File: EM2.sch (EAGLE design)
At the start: 114 parts, among them IC1 EUP3476SO08T, IC2 APX811-44UG-7, IC3 ATMEGA16U2-MU, IC4 MCP24AA025E48, IC6 W5500, IC9 ATMEGA2560-16AU, J1 DC_2_1MM, P1 USB-6PSMT, P3 ICSP:USB, P4 microSD, Q2 2N7002, U1 HY931147C-RJ45, X1 16MHz, X2 25MHz, X3 16MHz

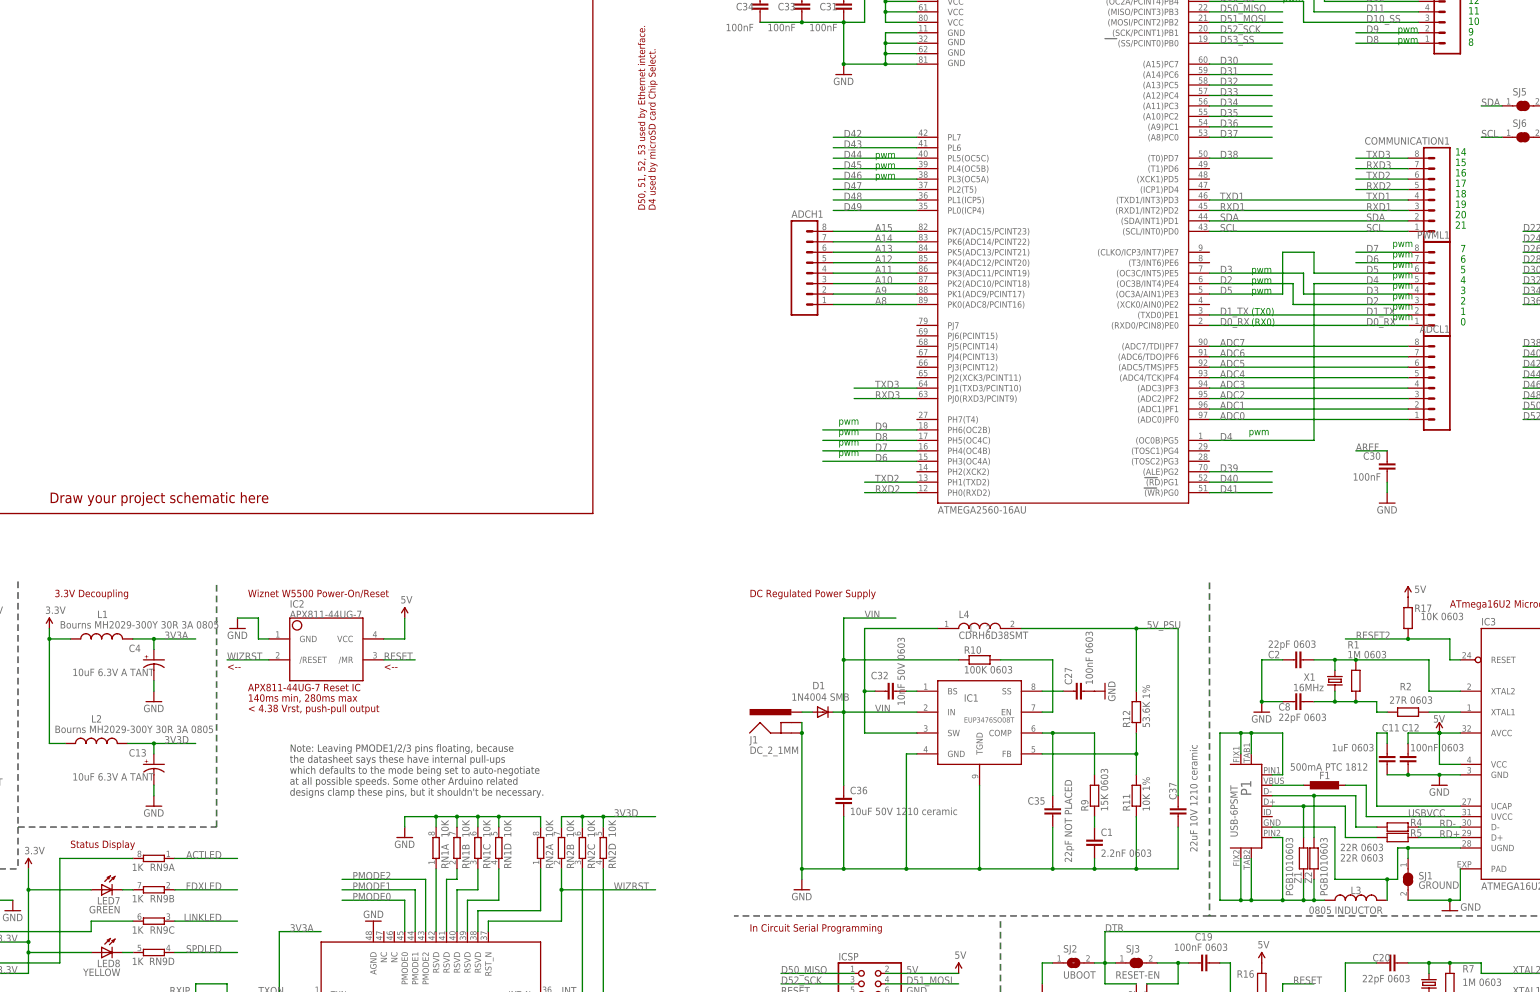
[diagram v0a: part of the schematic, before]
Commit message: Changed USB socket
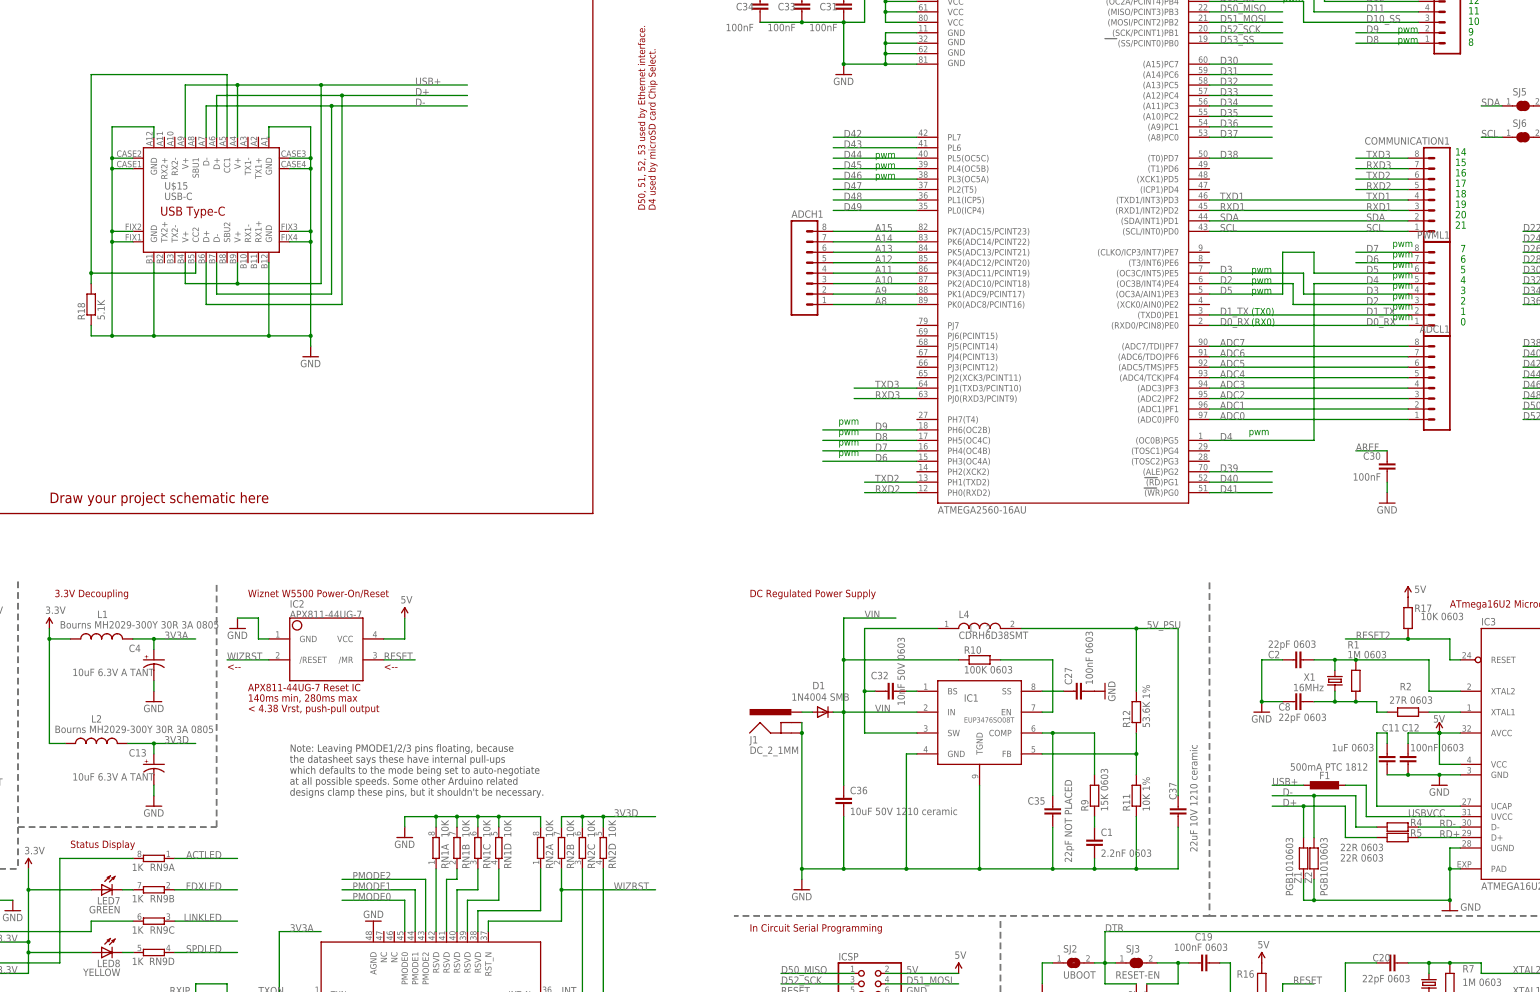
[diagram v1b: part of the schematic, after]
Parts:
- removed L3: 0805 INDUCTOR, freetronics-master-v1:INDUCTOR0805-LARGE
- removed P1: USB-6PSMT, freetronics-jon:USB-6PSMT
- removed SJ1: GROUND, freetronics-jon:SJCN
- added R18: 5.1K, freetronics-original:RESISTOR0603
- added U$15: USB-C, freetronics-jon:USB-C
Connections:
- removed net N$115: F1.1, P1.VBUS
- removed net N$16: P1.D+, R5.2, Z1.1
- removed net N$17: P1.D-, R4.2, Z2.1
- removed net N$18: L3.1, P1.FIX1, P1.FIX2, P1.PIN1, P1.PIN2, P1.TAB1, P1.TAB2, Z1.2, Z2.2
- removed net N$74: IC3.UGND, L3.2, P1.GND, SJ1.1
- new net D+: R5.2, U$15.D+@A6, U$15.D+@B6, Z1.1
- new net D-: R4.2, U$15.D-@A7, U$15.D-@B7, Z2.1
- new net N$67: R18.2, U$15.CC1, U$15.CC2
- new net USB+: F1.1, U$15.V+@A4, U$15.V+@A9, U$15.V+@B4, U$15.V+@B9
- net GND: now also IC3.UGND, R18.1, U$15.GND@A1, U$15.GND@A12, U$15.GND@B1, U$15.GND@B12, U$15.GND@CASE1, U$15.GND@CASE2, U$15.GND@CASE3, U$15.GND@CASE4, U$15.GND@FIX1, U$15.GND@FIX2, U$15.GND@FIX3, U$15.GND@FIX4, Z1.2, Z2.2; no longer SJ1.2

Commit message: Library part migration to SuperHouse
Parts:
- added R19: 5.1K, SuperHouse-DiscreteSemi:RESISTOR0603
- ADCH1, ADCL1, COMMUNICATION1, JP6, PWML1: value (none) -> M08-SOCKET; device freetronics-master-v1.1:M08STD -> SuperHouse-Connectors:M08-SOCKET
- C1, C12, C15, C16, C19, C2, C20, C21, C22, C23, C24, C27, C29, C30, C31, C32, C33, C34, C35, C7, C8, C9: device freetronics-marc:CAP0603 -> SuperHouse-DiscreteSemi:CAP0603
- C11: device freetronics-master-v1:CAP0603 -> SuperHouse-DiscreteSemi:CAP0603
- C14, C17, C5: device freetronics-jon:CAP0603 -> SuperHouse-DiscreteSemi:CAP0603
- D1: value 1N4004 SMB -> 1N4004 SMA; device freetronics:DIODESMB -> SuperHouse-DiscreteSemi:DIODESMA
- F1: device rcl:L-EUL1812 -> SuperHouse-Fuses:PTC050
- IC6: device W5500:W5500 -> SuperHouse-ICs:W5500
- IC9: device atmel-2005:ATMEGA1280-16AU -> SuperHouse-MCUs:ATMEGA25602560-16AU
- ICSP, P3: device pinhead:PINHD-2X3 -> SuperHouse-Connectors:ICSP-PIN
- J1: device freetronics-jon:POWER_JACKPTH_SLOTS -> SuperHouse-Connectors:POWER_JACK-SLOTS
- JP5: device freetronics-master-v1.1:M03PTH -> SuperHouse-Connectors:M03-PIN
- LED10, LED2, LED5, LED6, LED7, LED8: device freetronics-jon:LED0603 -> SuperHouse-LEDs:LED0603
- PWMH: value M100.1 -> M10-SOCKET; device freetronics-original:M100.1 -> SuperHouse-Connectors:M10-SOCKET
- Q2: device freetronics:MOSFET-NCHANNELSMD -> SuperHouse-DiscreteSemi:MOSFET-NCHANNEL-233
- R1, R13, R16, R17, R2, R22, R3, R4, R5, R6, R7, R8: device freetronics-marc:RESISTOR0603 -> SuperHouse-DiscreteSemi:RESISTOR0603
- R10, R11, R12, R18, R9: device freetronics-original:RESISTOR0603 -> SuperHouse-DiscreteSemi:RESISTOR0603
- R14, R15: device freetronics-master-v1.1:RESISTOR0603 -> SuperHouse-DiscreteSemi:RESISTOR0603
- RN1, RN2, RN9: device freetronics-master-v1.1:4R-NCAY16 -> SuperHouse-DiscreteSemi:4R-NCAY16
- RN3, RN5, RN6, RN8: device freetronics-master-v1:4R-NCAY16 -> SuperHouse-DiscreteSemi:4R-NCAY16
- S1: device freetronics:TAC_SWITCHSMD -> SuperHouse-Switches:TAC_SWITCH-SMT-6
- U$15: device freetronics-jon:USB-C -> SuperHouse-Connectors:USB-C
- U1: device freetronics-jon:HY931147C-RJ45 -> SuperHouse-Connectors:HY931147C-RJ45
- X1, X2, X3: device freetronics-master-v1:CRYSTALHC49UV -> SuperHouse-Oscillators:CRYSTALHC49UV
- Z1, Z2: device freetronics:RESISTOR0603 -> SuperHouse-DiscreteSemi:TVS0603
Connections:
- new net N$14: R18.2, U$15.CC2
- net GND: now also R19.1
- net N$67: now also R19.2; no longer R18.2, U$15.CC2
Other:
- note added: "EtherMega2 (Arduino Compatible)"
- note added: "www.superhouse.tv/em2"
- note removed: "Freetronics EtherMega2 (Arduino Compatible)"
- note removed: "www.freetronics.com.au/em2"
- moved on the sheet: ADCH1, ADCL1, COMMUNICATION1, PWML1
